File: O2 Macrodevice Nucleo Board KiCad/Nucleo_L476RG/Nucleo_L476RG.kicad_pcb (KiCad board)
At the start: 2 copper layers, 12 parts, among them J1 TS-108-T-A-1, J2 TS-108-T-A-1, U1 STM32L476RGTx, X1 ABS25-32.768KHZ-6-T

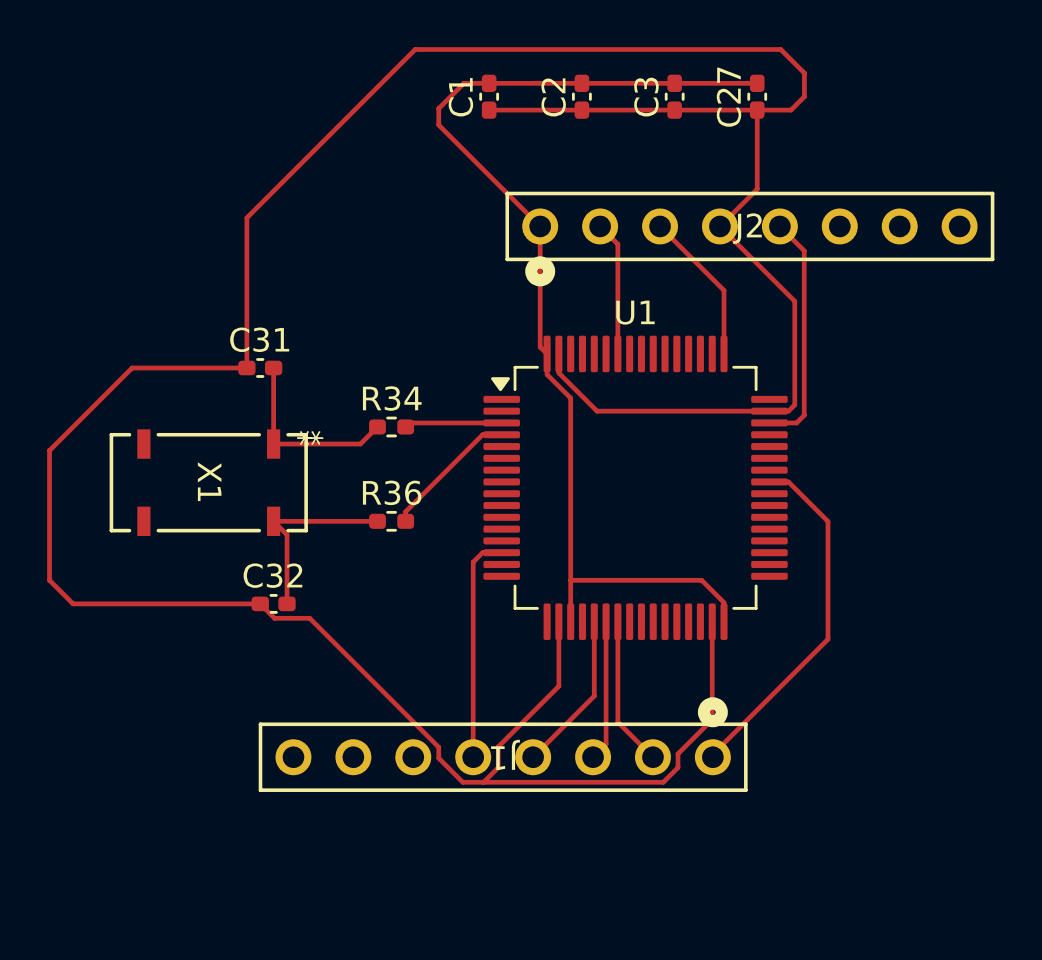
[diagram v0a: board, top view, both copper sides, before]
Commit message: updated NFC and Nucleo boards with new SMD header connectors
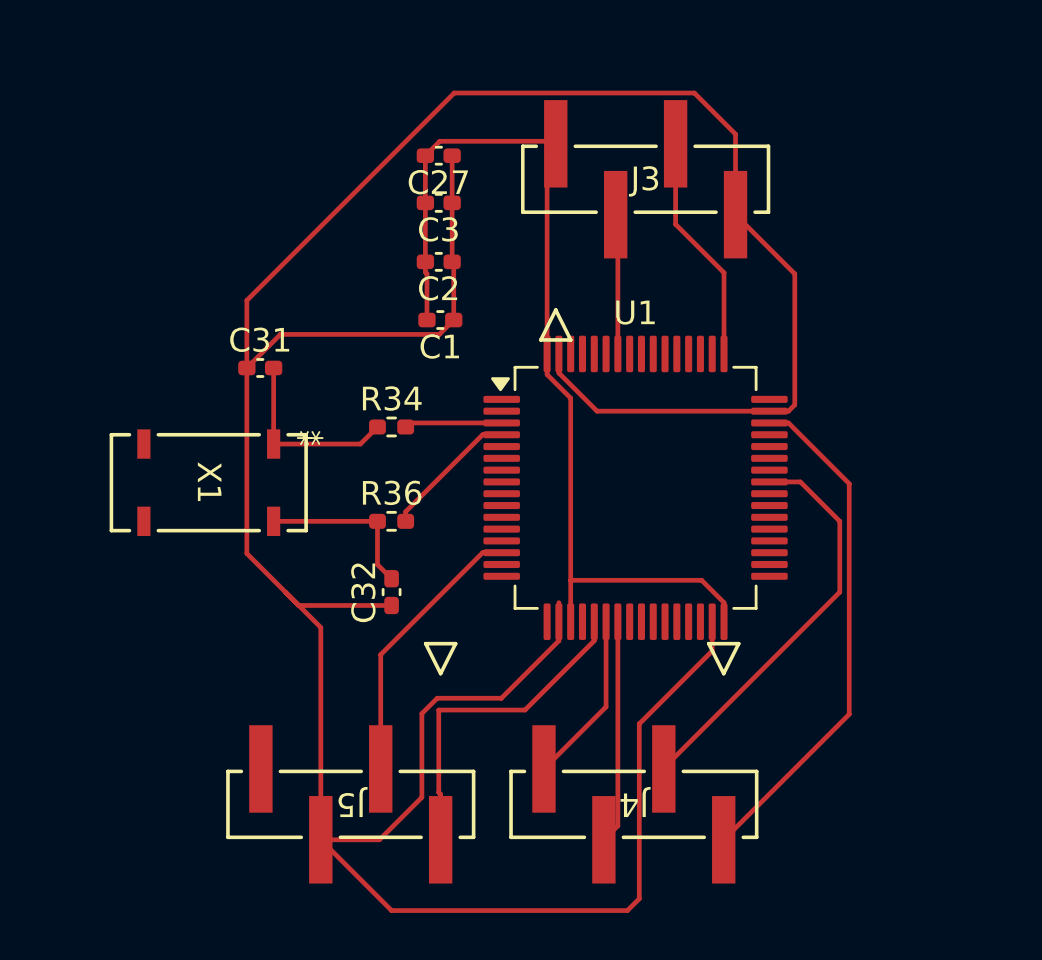
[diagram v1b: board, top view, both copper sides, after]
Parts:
- removed J1, J2: TS-108-T-A-1, Header_Connector:CON8_1X8_TUC_HTS_SAI
- added J3: 61000418221, SMD Header:61000418221_WRE, F.Cu at (145.3, 77.5)
- added J4: 61000418221, SMD Header:61000418221_WRE, F.Cu at (144.8, 104.0)
- added J5: 61000418221, SMD Header:61000418221_WRE, F.Cu at (132.8, 104.0)
- moved C27 13.7 mm to (136.5, 76.5), turned to 180 degrees
- moved C3 11.0 mm to (136.5, 78.5), turned to 180 degrees
- moved C1 9.69 mm to (136.6, 83.5), turned to 180 degrees
- moved C2 9.26 mm to (136.5, 81.0), turned to 180 degrees
- moved C32 5.02 mm to (134.5, 95.0), turned to 90 degrees
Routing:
- net /SWDIO: track 10.0 -> 21.7 mm
- net /SCK: track 6.82 -> 14.1 mm
- net GND: track 135.0 -> 139.9 mm
- net /<NO NET>: track 45.7 -> 41.3 mm
- net /SWCLK: track 6.53 -> 9.76 mm
- net /MOSI: track 6.36 -> 9.49 mm
- net /GPIO_EXTIO: track 9.64 -> 11.8 mm
- net /TX_TP: track 15.4 -> 17.3 mm
- net /MISO: track 5.97 -> 7.33 mm
- net Net-(C32-Pad2): track 8.14 -> 7.08 mm
